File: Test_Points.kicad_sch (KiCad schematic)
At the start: 2 parts, among them J5 Power test points

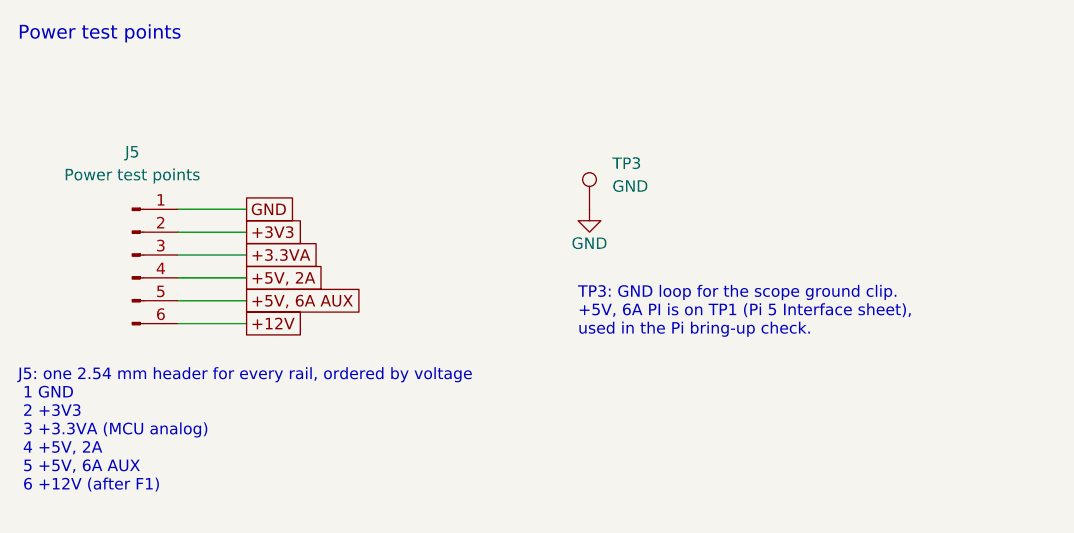
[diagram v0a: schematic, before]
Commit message: Rename power nets, add mounting holes, retitle sheet 1, clear ERC
Power nets, no commas, named by function:
- "+5V, 2A" -> +5V_SYS, "+5V, 6A PI" -> +5V_PI, "+5V, 6A AUX" -> +5V_AUX
Buck sheets renamed to Buck 5V SYS / Buck 5V PI / Buck 5V AUX. Notes,
descriptions, README and docs updated.

Mechanical and title:
- H1-H4: M3 mounting holes, 3.2 mm plated, isolated (no net), not in BOM
- Sheet 1 title: "Delivery Robot Main Board"

ERC, now 0 errors and 0 warnings (was 4 errors, 15 warnings):
- PWR_FLAGs on +12V (after F1), GND (at J2), +3.3VA (after FB2) and
  +5V_SYS (after the TPS54202's L1)
- TPSM63606 symbol pin types set (VOUT power out, FB/EN input, VIN/
  VLDOIN/GND power in, PG open collector, others passive) in both buck
  sheets and libs/TPSM63606RDLR.kicad_sym
- U1 STM32F091RCTx and Y3 Crystal_GND24 moved to a new
  libs/project_symbols.kicad_sym holding the versions this design uses
  (the current KiCad library moved their pins); libs/TPS54202DDCR made
  to match the schematic's U3
Connectivity unchanged: same 108 nets and pins.

Co-Authored-By: Claude Opus 5.5 <noreply@anthropic.com>
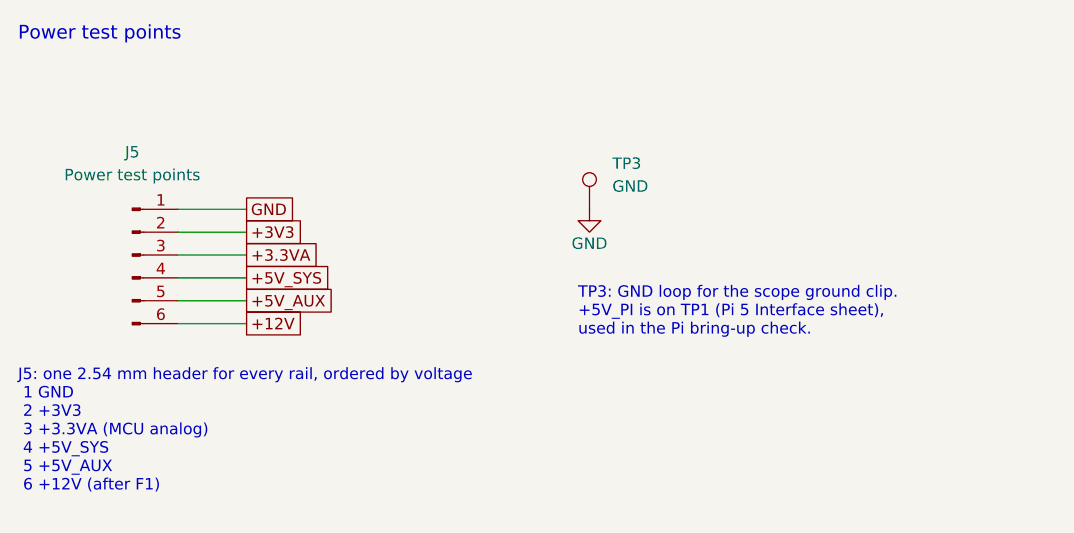
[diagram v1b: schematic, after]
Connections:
- net +5V, 2A renamed +5V_SYS
- net +5V, 6A AUX renamed +5V_AUX
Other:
- note added: "J5: one 2.54 mm header for every rail, ordered by voltage 1 GND 2 +3V3 3 +3.3VA (MCU analog) 4 +5V_SYS 5 +5V_AUX 6 +12V (after F1)"
- note added: "TP3: GND loop for the scope ground clip. +5V_PI is on TP1 (Pi 5 Interface sheet), used in the Pi bring-up check."
- note removed: "J5: one 2.54 mm header for every rail, ordered by voltage 1 GND 2 +3V3 3 +3.3VA (MCU analog) 4 +5V, 2A 5 +5V, 6A AUX 6 +12V (after F1)"
- note removed: "TP3: GND loop for the scope ground clip. +5V, 6A PI is on TP1 (Pi 5 Interface sheet), used in the Pi bring-up check."
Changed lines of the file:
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@@
 		(company "Senior Design")
 	)
-	(text "J5: one 2.54 mm header for every rail, ordered by voltage\n 1 GND\n 2 +3V3\n 3 +3.3VA (MCU analog)\n 4 +5V, 2A\n 5 +5V, 6A AUX\n 6 +12V (after F1)"
+	(text "J5: one 2.54 mm header for every rail, ordered by voltage\n 1 GND\n 2 +3V3\n 3 +3.3VA (MCU analog)\n 4 +5V_SYS\n 5 +5V_AUX\n 6 +12V (after F1)"
 		(exclude_from_sim no)
 		(at 38.1 76.2 0)
@@
 		)
 	)
-	(text "TP3: GND loop for the scope ground clip.\n+5V, 6A PI is on TP1 (Pi 5 Interface sheet),\nused in the Pi bring-up check."
+	(text "TP3: GND loop for the scope ground clip.\n+5V_PI is on TP1 (Pi 5 Interface sheet),\nused in the Pi bring-up check."
 		(exclude_from_sim no)
 		(at 100.33 67.056 0)
@@
 		)
 	)
-	(global_label "+5V, 6A AUX"
+	(global_label "+5V_AUX"
 		(shape passive)
 		(at 63.5 68.58 0)
@@
 		)
 	)
-	(global_label "+5V, 2A"
+	(global_label "+5V_SYS"
 		(shape passive)
 		(at 63.5 66.04 0)
@@
 			)
 		)
-		(property "Description" "Power test header, 2.54 mm male 1x06: 1 = GND, 2 = +3V3, 3 = +3.3VA, 4 = +5V, 2A, 5 = +5V, 6A AUX, 6 = +12V (after F1). Rails ordered by voltage with GND at pin 1 and +12V at pin 6."
+		(property "Description" "Power test header, 2.54 mm male 1x06: 1 = GND, 2 = +3V3, 3 = +3.3VA, 4 = +5V_SYS, 5 = +5V_AUX, 6 = +12V (after F1). Rails ordered by voltage with GND at pin 1 and +12V at pin 6."
 			(at 50.8 63.5 0)
 			(hide yes)

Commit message: Add input protection, AUX ports, servo interface and Pi control
Implements the 2026-10-15 design review decisions in the schematic.
ERC 0 errors, 0 warnings.

New sheets:
- Input Protection: Q1 SQJ409EP reverse-battery P-FET after F1 (D12
  12 V gate clamp, R36), D13 SMBJ16A TVS on +12V, battery sense
  R37/R38/C37 -> VBAT_SENSE on PA0. PWR_FLAG moves to +12V.
- AUX Outputs: four +5V_AUX ports J18-J21 (JST XH 2-pin: Notecard,
  LiDAR, GNSS, IMU), each through a 1.5 A PTC (F4-F7).
- Servo Interface: J17 (GND, VBAT_SERVO via F3 5 A fuse, SERVO_SIG) for
  the Hiwonder HTS-30HS through an external 11.1-12 V buck. U8
  SN74LVC1T45 translates PB10 (USART3 half-duplex) to the 5 V bus,
  PB11 sets direction; R39-R42 pull-ups/series, D14 ESD.

Root sheet:
- F1 output is now VBAT_FUSED; C36 sits on +12V after Q1. J2-F1 net
  named VBAT_IN. F1 7.5 A -> 10 A (0297010.L).
- Y3/C5/C6 fitted (were DNP).
- PA0 -> VBAT_SENSE, PA1 -> PI_3V3_SENSE, PB10 -> SERVO_TX,
  PB11 -> SERVO_DIR. Notes updated (no more F2 / XT30-only text).

Pi 5 Interface:
- J13 -> 6-pin JST XH: TXD, RXD, GND, PI_3V3, PI_RESET, PI_BOOT0.
- PI_3V3 -> D15 -> AUX_EN (U5 enable) and R44/R45 -> PA1.
- PI_RESET -> Q2 DMN63D8L -> NRST (open drain, R46 pull-down).
- PI_BOOT0 -> R47 1k -> BOOT0, for reflashing over USART2.
- R12/R13 100R -> 1k (PA2/PA3 are TTa, 5 mA injection max).
- Remove TP2 (same net as TP1 since F2 was removed).

Buck 5V AUX: U5 EN from AUX_EN (was +12V), R43 100k pull-down, C40,
J22 force-on jumper. Buck 5V SYS: C49 100 nF at U3 VIN/GND.
U2/U5 value TPSM63606RDLR; VCC design note corrected (internal 1 uF,
must stay NC).

Motor Control (now A3):
- U9/U10 74LVC2G17 encoder buffers on +3V3; encoder series R 100R ->
  1k with C43-C46 1 nF; R48-R51 4.7k pull-ups (DNP).
- F8/F9 0.2 A PTC + C47/C48 on each encoder supply (ENC1_5V, ENC2_5V).
- J7/J15 pin order 5V, GND, A, B (matches the am-3651 plug).
- R52/R53 10k pull-downs on both PWM lines (MDD20A brakes on low).
- F10/F11 PTC in series with J6/J16 p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
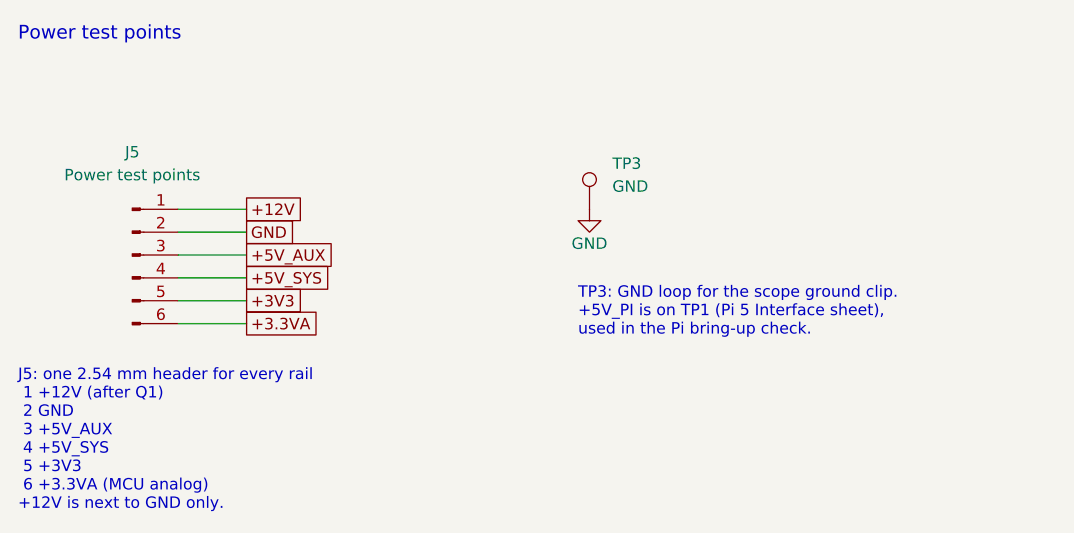
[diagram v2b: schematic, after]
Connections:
- net +12V: now also J5.1 (Pin_1); no longer J5.6 (Pin_6)
- net +3.3VA: now also J5.6 (Pin_6); no longer J5.3 (Pin_3)
- net +3V3: now also J5.5 (Pin_5); no longer J5.2 (Pin_2)
- net +5V_AUX: now also J5.3 (Pin_3); no longer J5.5 (Pin_5)
- net GND: now also J5.2 (Pin_2); no longer J5.1 (Pin_1)
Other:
- note added: "J5: one 2.54 mm header for every rail 1 +12V (after Q1) 2 GND 3 +5V_AUX 4 +5V_SYS 5 +3V3 6 +3.3VA (MCU analog) +12V is next to GND only."
- note removed: "J5: one 2.54 mm header for every rail, ordered by voltage 1 GND 2 +3V3 3 +3.3VA (MCU analog) 4 +5V_SYS 5 +5V_AUX 6 +12V (after F1)"
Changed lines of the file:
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@@
 		(company "Senior Design")
 	)
-	(text "J5: one 2.54 mm header for every rail, ordered by voltage\n 1 GND\n 2 +3V3\n 3 +3.3VA (MCU analog)\n 4 +5V_SYS\n 5 +5V_AUX\n 6 +12V (after F1)"
+	(text "J5: one 2.54 mm header for every rail\n 1 +12V (after Q1)\n 2 GND\n 3 +5V_AUX\n 4 +5V_SYS\n 5 +3V3\n 6 +3.3VA (MCU analog)\n+12V is next to GND only."
 		(exclude_from_sim no)
 		(at 38.1 76.2 0)
@@
 		)
 	)
+	(global_label "+3V3"
+		(shape passive)
+		(at 63.5 68.58 0)
+		(fields_autoplaced yes)
+		(effects
+			(font
+				(size 1.27 1.27)
+			)
+			(justify left)
+		)
+		(property "Intersheetrefs" "${INTERSHEET_REFS}"
+			(at 63.5 68.58 0)
+			(hide yes)
+			(show_name no)
+			(do_not_autoplace no)
+			(effects
+				(font
+					(size 1.27 1.27)
+				)
+			)
+		)
+	)
+	(global_label "+12V"
+		(shape passive)
+		(at 63.5 58.42 0)
+		(fields_autoplaced yes)
+		(effects
+			(font
+				(size 1.27 1.27)
+			)
+			(justify left)
+		)
+		(property "Intersheetrefs" "${INTERSHEET_REFS}"
+			(at 63.5 58.42 0)
+			(hide yes)
+			(show_name no)
+			(do_not_autoplace no)
+			(effects
+				(font
+					(size 1.27 1.27)
+				)
+			)
+		)
+	)
+	(global_label "+5V_SYS"
+		(shape passive)
+		(at 63.5 66.04 0)
+		(fields_autoplaced yes)
+		(effects
+			(font
+				(size 1.27 1.27)
+			)
+			(justify left)
+		)
+		(property "Intersheetrefs" "${INTERSHEET_REFS}"
+			(at 63.5 66.04 0)
+			(hide yes)
+			(show_name no)
+			(do_not_autoplace no)
+			(effects
+				(font
+					(size 1.27 1.27)
+				)
+			)
+		)
+	)
+	(global_label "+3.3VA"
+		(shape passive)
+		(at 63.5 71.12 0)
+		(fields_autoplaced yes)
+		(effects
+			(font
+				(size 1.27 1.27)
+			)
+			(justify left)
+		)
+		(property "Intersheetrefs" "${INTERSHEET_REFS}"
+			(at 63.5 71.12 0)
+			(hide yes)
+			(show_name no)
+			(do_not_autoplace no)
+			(effects
+				(font
+					(size 1.27 1.27)
+				)
+			)
+		)
+	)
+	(global_label "GND"
+		(shape passive)
+		(at 63.5 60.96 0)
+		(fields_autoplaced yes)
+		(effects
+			(font
+				(size 1.27 1.27)
+			)
+			(justify left)
+		)
+		(property "Intersheetrefs" "${INTERSHEET_REFS}"
+			(at 63.5 60.96 0)
+			(hide yes)
+			(show_name no)
+			(do_not_autoplace no)
+			(effects
+				(font
+					(size 1.27 1.27)
+				)
+			)
+		)
+	)
 	(global_label "+5V_AUX"
-		(shape passive)
-		(at 63.5 68.58 0)
-		(fields_autoplaced yes)
-		(effects
-			(font
-				(size 1.27 1.27)
-			)
-			(justify left)
-		)
-		(property "Intersheetrefs" "${INTERSHEET_REFS}"
-			(at 63.5 68.58 0)
-			(hide yes)
-			(show_name no)
-			(do_not_autoplace no)
-			(effects
-				(font
-					(size 1.27 1.27)
-				)
-			)
-		)
-	)
-	(global_label "GND"
-		(shape passive)
-		(at 63.5 58.42 0)
-		(fields_autoplaced yes)
-		(effects
-			(font
-				(size 1.27 1.27)
-			)
-			(justify left)
-		)
-		(property "Intersheetrefs" "${INTERSHEET_REFS}"
-			(at 63.5 58.42 0)
-			(hide yes)
-			(show_name no)
-			(do_not_autoplace no)
-			(effects
-				(font
-					(size 1.27 1.27)
-				)
-			)
-		)
-	)
-	(global_label "+5V_SYS"
-		(shape passive)
-		(at 63.5 66.04 0)
-		(fields_autoplaced yes)
-		(effects
-			(font
-				(size 1.27 1.27)
-			)
-			(justify left)
-		)
-		(property "Intersheetrefs" "${INTERSHEET_REFS}"
-			(at 63.5 66.04 0)
-			(hide yes)
-			(show_name no)
-			(do_not_autoplace no)
-			(effects
-				(font
-					(size 1.27 1.27)
-				)
-			)
-		)
-	)
-	(global_label "+12V"
-		(shape passive)
-		(at 63.5 71.12 0)
-		(fields_autoplaced yes)
-		(effects
-			(font
-				(size 1.27 1.27)
-			)
-			(justify left)
-		)
-		(property "Intersheetrefs" "${INTERSHEET_REFS}"
-			(at 63.5 71.12 0)
-			(hide yes)
-			(show_name no)
-			(do_not_autoplace no)
-			(effects
-				(font
-					(size 1.27 1.27)
-				)
-			)
-		)
-	)
-	(global_label "+3V3"
-		(shape passive)
-		(at 63.5 60.96 0)
-		(fields_autoplaced yes)
-		(effects
-			(font
-				(size 1.27 1.27)
-			)
-			(justify left)
-		)
-		(property "Intersheetrefs" "${INTERSHEET_REFS}"
-			(at 63.5 60.96 0)
-			(hide yes)
-			(show_name no)
-			(do_not_autoplace no)
-			(effects
-				(font
-					(size 1.27 1.27)
-				)
-			)
-		)
-	)
-	(global_label "+3.3VA"
 		(shape passive)
 		(at 63.5 63.5 0)
@@
 			)
 		)
-		(property "Description" "Power test header, 2.54 mm male 1x06: 1 = GND, 2 = +3V3, 3 = +3.3VA, 4 = +5V_SYS, 5 = +5V_AUX, 6 = +12V (after F1). Rails ordered by voltage with GND at pin 1 and +12V at pin 6."
+		(property "Description" "Power test header, 2.54 mm male 1x06: 1 = +12V (after Q1), 2 = GND, 3 = +5V_AUX, 4 = +5V_SYS, 5 = +3V3, 6 = +3.3VA. +12V sits next to GND only, so a slipped probe cannot put 12 V on a 5 V rail."
 			(at 50.8 63.5 0)
 			(hide yes)
